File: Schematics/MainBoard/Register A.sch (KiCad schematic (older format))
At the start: 5 parts, among them J8 A Register LED Connector, U65 74F377, U66 74LS245

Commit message: Pin swap register A and B bus transceivers to reverse order of pins and be consistent with rest of board.
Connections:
- net A0: now also U65.2 (Q0), U66.18 (B0); no longer U65.19 (Q7), U66.11 (B7)
- net A1: now also U65.5 (Q1), U66.17 (B1); no longer U65.16 (Q6), U66.12 (B6)
- net A2: now also U65.6 (Q2), U66.16 (B2); no longer U65.15 (Q5), U66.13 (B5)
- net A3: now also U65.9 (Q3), U66.15 (B3); no longer U65.12 (Q4), U66.14 (B4)
- net A4: now also U65.12 (Q4), U66.14 (B4); no longer U65.9 (Q3), U66.15 (B3)
- net A5: now also U65.15 (Q5), U66.13 (B5); no longer U65.6 (Q2), U66.16 (B2)
- net A6: now also U65.16 (Q6), U66.12 (B6); no longer U65.5 (Q1), U66.17 (B1)
- net A7: now also U65.19 (Q7), U66.11 (B7); no longer U65.2 (Q0), U66.18 (B0)
- net DataBus0: now also U65.3 (D0), U66.2 (A0); no longer U65.18 (D7), U66.9 (A7)
- net DataBus1: now also U65.4 (D1), U66.3 (A1); no longer U65.17 (D6), U66.8 (A6)
- net DataBus2: now also U65.7 (D2), U66.4 (A2); no longer U65.14 (D5), U66.7 (A5)
- net DataBus3: now also U65.8 (D3), U66.5 (A3); no longer U65.13 (D4), U66.6 (A4)
- net DataBus4: now also U65.13 (D4), U66.6 (A4); no longer U65.8 (D3), U66.5 (A3)
- net DataBus5: now also U65.14 (D5), U66.7 (A5); no longer U65.7 (D2), U66.4 (A2)
- net DataBus6: now also U65.17 (D6), U66.8 (A6); no longer U65.4 (D1), U66.3 (A1)
- net DataBus7: now also U65.18 (D7), U66.9 (A7); no longer U65.3 (D0), U66.2 (A0)
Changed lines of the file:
@@
 	8300 2100 8200 2200
 Text Label 7800 2300 0    50   ~ 0
+DataBus1
+Text Label 7800 2400 0    50   ~ 0
+DataBus2
+Text Label 7800 2500 0    50   ~ 0
+DataBus3
+Text Label 7800 2600 0    50   ~ 0
+DataBus4
+Text Label 7800 2700 0    50   ~ 0
+DataBus5
+Text Label 7800 2800 0    50   ~ 0
 DataBus6
-Text Label 7800 2400 0    50   ~ 0
-DataBus5
-Text Label 7800 2500 0    50   ~ 0
-DataBus4
-Text Label 7800 2600 0    50   ~ 0
-DataBus3
-Text Label 7800 2700 0    50   ~ 0
-DataBus2
-Text Label 7800 2800 0    50   ~ 0
-DataBus1
 Text Label 7800 2900 0    50   ~ 0
+DataBus7
+Text Label 7800 2200 0    50   ~ 0
 DataBus0
-Text Label 7800 2200 0    50   ~ 0
-DataBus7
 $Comp
 L Device:C C?
@@
 	3100 2100 3200 2200
 Text Label 3600 2300 2    50   ~ 0
+DataBus1
+Text Label 3600 2400 2    50   ~ 0
+DataBus2
+Text Label 3600 2500 2    50   ~ 0
+DataBus3
+Text Label 3600 2600 2    50   ~ 0
+DataBus4
+Text Label 3600 2700 2    50   ~ 0
+DataBus5
+Text Label 3600 2800 2    50   ~ 0
 DataBus6
-Text Label 3600 2400 2    50   ~ 0
-DataBus5
-Text Label 3600 2500 2    50   ~ 0
-DataBus4
-Text Label 3600 2600 2    50   ~ 0
-DataBus3
-Text Label 3600 2700 2    50   ~ 0
-DataBus2
-Text Label 3600 2800 2    50   ~ 0
-DataBus1
 Text Label 3600 2900 2    50   ~ 0
+DataBus7
+Text Label 3600 2200 2    50   ~ 0
 DataBus0
-Text Label 3600 2200 2    50   ~ 0
-DataBus7
 Wire Wire Line
 	3200 2900 4150 2900
@@
 	8950 1650 5600 1650
 Text Label 5450 2900 2    50   ~ 0
+A7
+Text Label 5450 2800 2    50   ~ 0
+A6
+Text Label 5450 2700 2    50   ~ 0
+A5
+Text Label 5450 2600 2    50   ~ 0
+A4
+Text Label 5450 2500 2    50   ~ 0
+A3
+Text Label 5450 2400 2    50   ~ 0
+A2
+Text Label 5450 2300 2    50   ~ 0
+A1
+Text Label 5450 2200 2    50   ~ 0
 A0
-Text Label 5450 2800 2    50   ~ 0
-A1
-Text Label 5450 2700 2    50   ~ 0
-A2
-Text Label 5450 2600 2    50   ~ 0
-A3
-Text Label 5450 2500 2    50   ~ 0
-A4
-Text Label 5450 2400 2    50   ~ 0
-A5
-Text Label 5450 2300 2    50   ~ 0
-A6
-Text Label 5450 2200 2    50   ~ 0
-A7
 Wire Wire Line
 	2700 3500 2700 3800
@@
 Entry Wire Line
 	4000 5100 3900 5000
-Wire Bus Line
-	5600 1650 5600 2800
 Wire Wire Line
 	7250 3200 7500 3200
@@
 Wire Wire Line
 	2700 3800 7500 3800
-Wire Wire Line
-	5150 2900 6250 2900
-Wire Wire Line
-	5150 2300 6250 2300
-Wire Wire Line
-	5150 2400 6250 2400
-Wire Wire Line
-	5150 2500 6250 2500
-Wire Wire Line
-	5150 2600 6250 2600
-Wire Wire Line
-	5150 2700 6250 2700
-Wire Wire Line
-	5150 2800 6250 2800
-Wire Wire Line
-	5150 2200 6250 2200
-Wire Bus Line
-	3100 1900 3100 2800
-Wire Bus Line
-	8300 1800 8300 2800
-Wire Bus Line
-	3350 5000 4300 5000
 $Comp
 L power:GND #PWR?
@@
 	0    -1   -1   0
 $EndComp
+Wire Wire Line
+	5150 2900 6250 2900
+Wire Wire Line
+	5150 2300 6250 2300
+Wire Wire Line
+	5150 2400 6250 2400
+Wire Wire Line
+	5150 2500 6250 2500
+Wire Wire Line
+	5150 2600 6250 2600
+Wire Wire Line
+	5150 2700 6250 2700
+Wire Wire Line
+	5150 2800 6250 2800
+Wire Wire Line
+	5150 2200 6250 2200
+Wire Bus Line
+	5600 1650 5600 2800
+Wire Bus Line
+	3100 1900 3100 2800
+Wire Bus Line
+	8300 1800 8300 2800
+Wire Bus Line
+	3350 5000 4300 5000
 $EndSCHEMATC

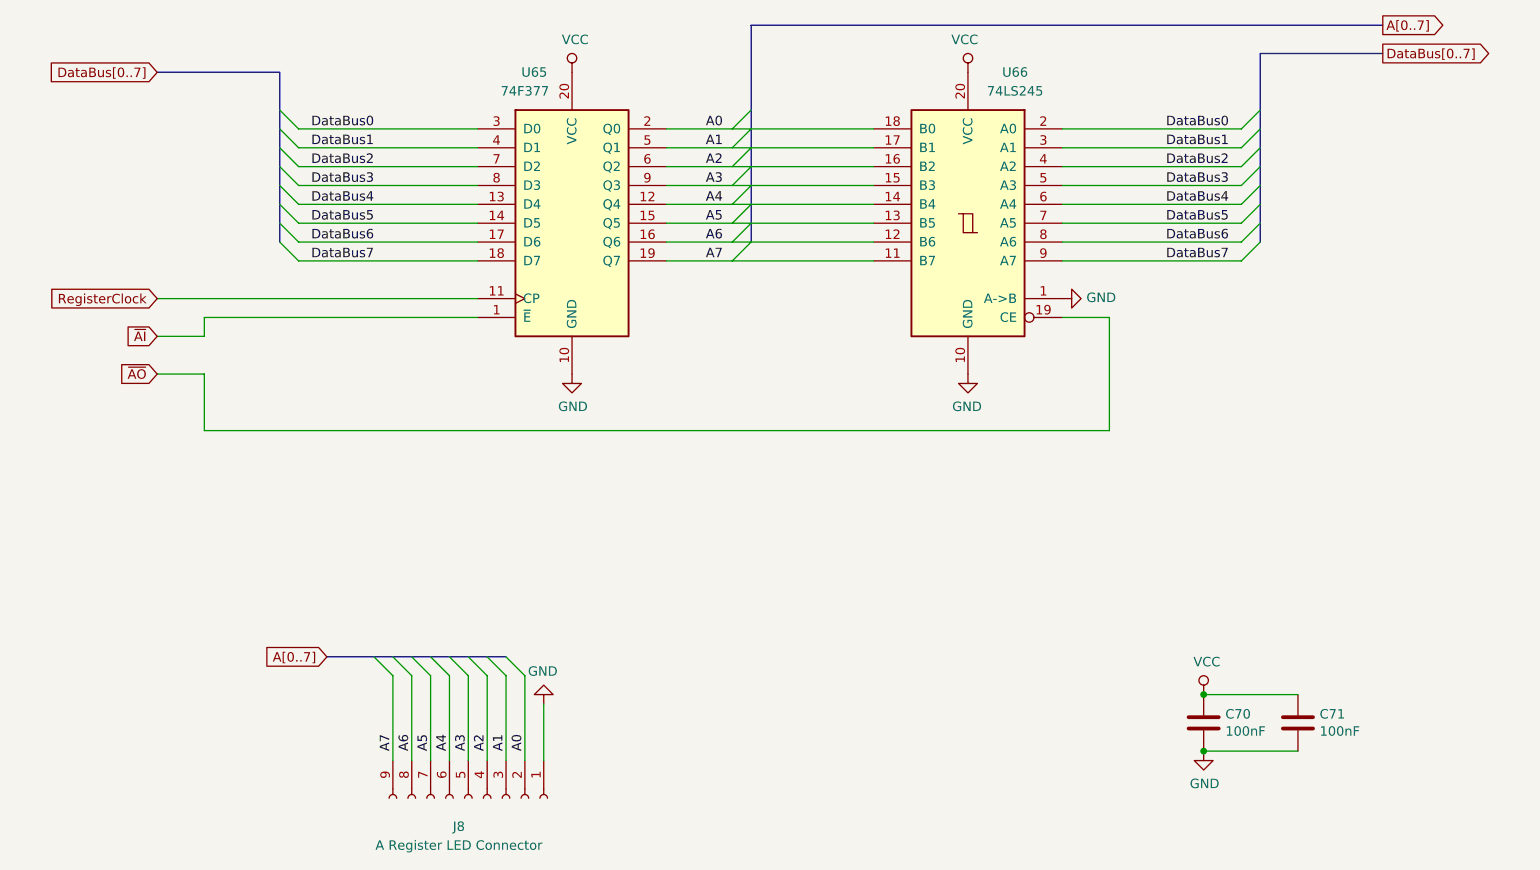
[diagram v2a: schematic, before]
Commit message: Connect together the data bus along the middle of the board.
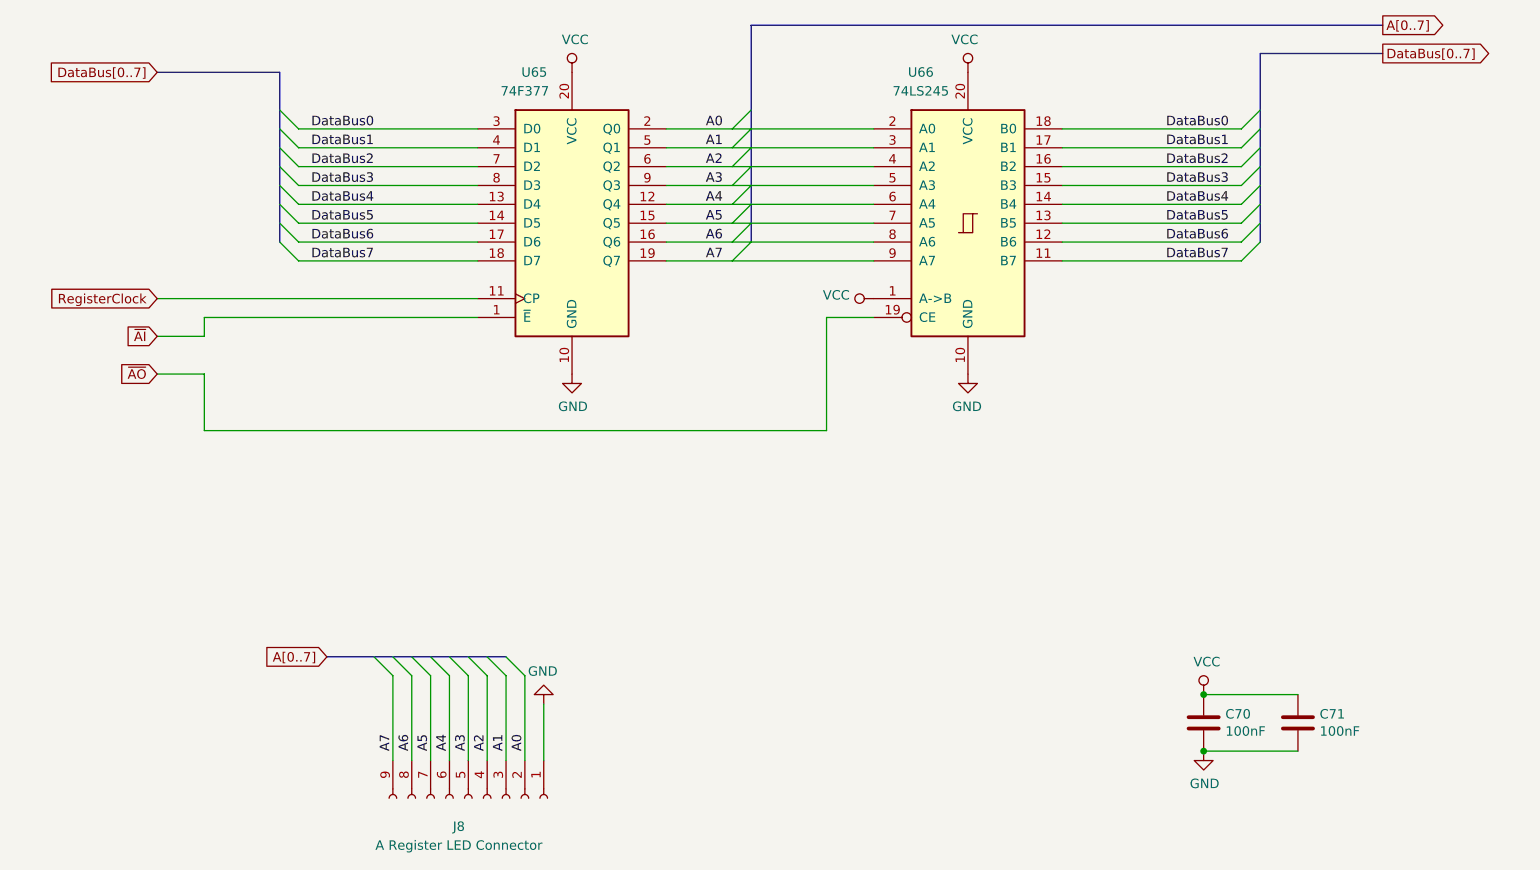
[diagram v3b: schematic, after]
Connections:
- net A0: now also U66.2 (A0); no longer U66.18 (B0)
- net A1: now also U66.3 (A1); no longer U66.17 (B1)
- net A2: now also U66.4 (A2); no longer U66.16 (B2)
- net A3: now also U66.5 (A3); no longer U66.15 (B3)
- net A4: now also U66.6 (A4); no longer U66.14 (B4)
- net A5: now also U66.7 (A5); no longer U66.13 (B5)
- net A6: now also U66.8 (A6); no longer U66.12 (B6)
- net A7: now also U66.9 (A7); no longer U66.11 (B7)
- net DataBus0: now also U66.18 (B0); no longer U66.2 (A0)
- net DataBus1: now also U66.17 (B1); no longer U66.3 (A1)
- net DataBus2: now also U66.16 (B2); no longer U66.4 (A2)
- net DataBus3: now also U66.15 (B3); no longer U66.5 (A3)
- net DataBus4: now also U66.14 (B4); no longer U66.6 (A4)
- net DataBus5: now also U66.13 (B5); no longer U66.7 (A5)
- net DataBus6: now also U66.12 (B6); no longer U66.8 (A6)
- net DataBus7: now also U66.11 (B7); no longer U66.9 (A7)
- net GND: no longer U66.1 (A->B)
- net VCC: now also U66.1 (A->B)
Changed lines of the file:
@@
 F 3 "http://www.ti.com/lit/gpn/sn74LS245" H 6750 2700 50  0001 C CNN
 	1    6750 2700
-	-1   0    0    -1
+	1    0    0    -1
 $EndComp
 $Comp
@@
 	4000 5100 3900 5000
 Wire Wire Line
-	7250 3200 7500 3200
-Wire Wire Line
-	7500 3200 7500 3800
-Wire Wire Line
-	2700 3800 7500 3800
-$Comp
-L power:GND #PWR0198
-U 1 1 5D99567A
-P 7250 3100
-F 0 "#PWR0198" H 7250 2850 50  0001 C CNN
-F 1 "GND" V 7255 2972 50  0000 R CNN
-F 2 "" H 7250 3100 50  0001 C CNN
-F 3 "" H 7250 3100 50  0001 C CNN
-	1    7250 3100
+	2700 3800 6000 3800
+Wire Bus Line
+	5600 1650 5600 2800
+$Comp
+L power:VCC #PWR?
+U 1 1 5D9A9CB2
+P 6250 3100
+F 0 "#PWR?" H 6250 2950 50  0001 C CNN
+F 1 "VCC" V 6268 3227 50  0000 L CNN
+F 2 "" H 6250 3100 50  0001 C CNN
+F 3 "" H 6250 3100 50  0001 C CNN
+	1    6250 3100
 	0    -1   -1   0
 $EndComp
 Wire Wire Line
+	6250 3200 6000 3200
+Wire Wire Line
+	6000 3200 6000 3800
+Wire Wire Line
 	5150 2900 6250 2900
 Wire Wire Line
@@
 	5150 2200 6250 2200
 Wire Bus Line
-	5600 1650 5600 2800
-Wire Bus Line
 	3100 1900 3100 2800
